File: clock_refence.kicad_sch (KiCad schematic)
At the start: 132 parts, among them J201 REFIN, J202 REFIN_DIRECT_P, J203 REFIN_DIRECT_N, J204 REFOUT_AUX_P, J205 REFOUT_AUX_N, J206 RFShield_TwoPieces, J207 REFOUT, J208 VTUNE, J209 DNP, T201 TC2-1T+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

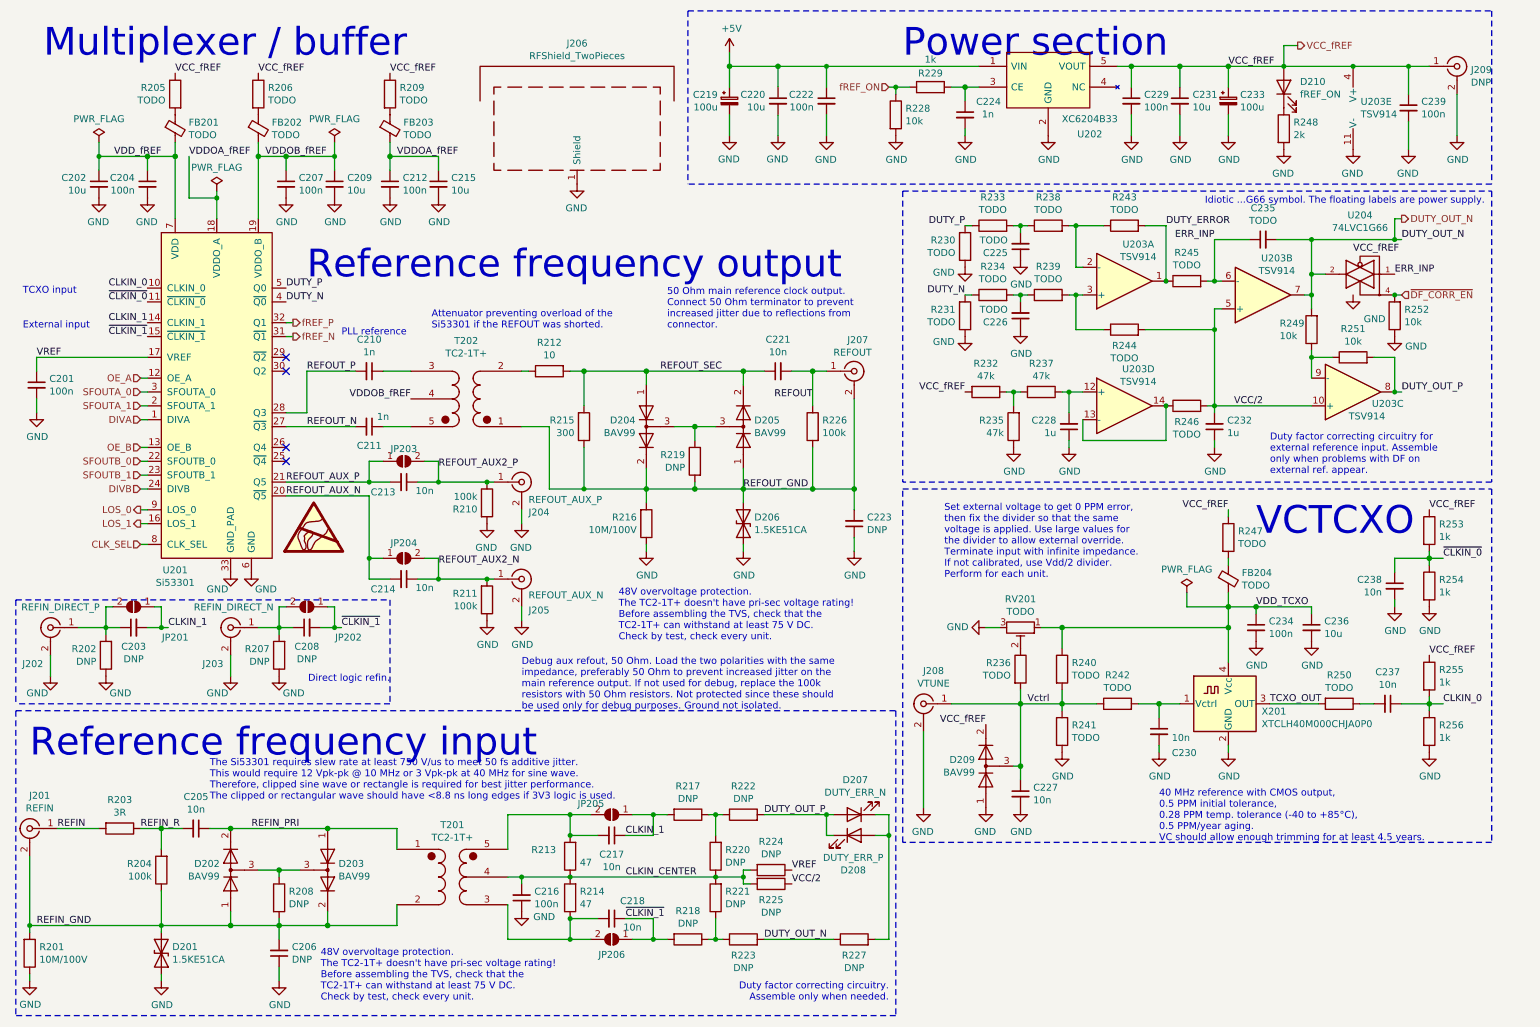
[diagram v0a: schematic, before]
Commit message: Working on making the original module a self-contained module with MCU. Added PCB.
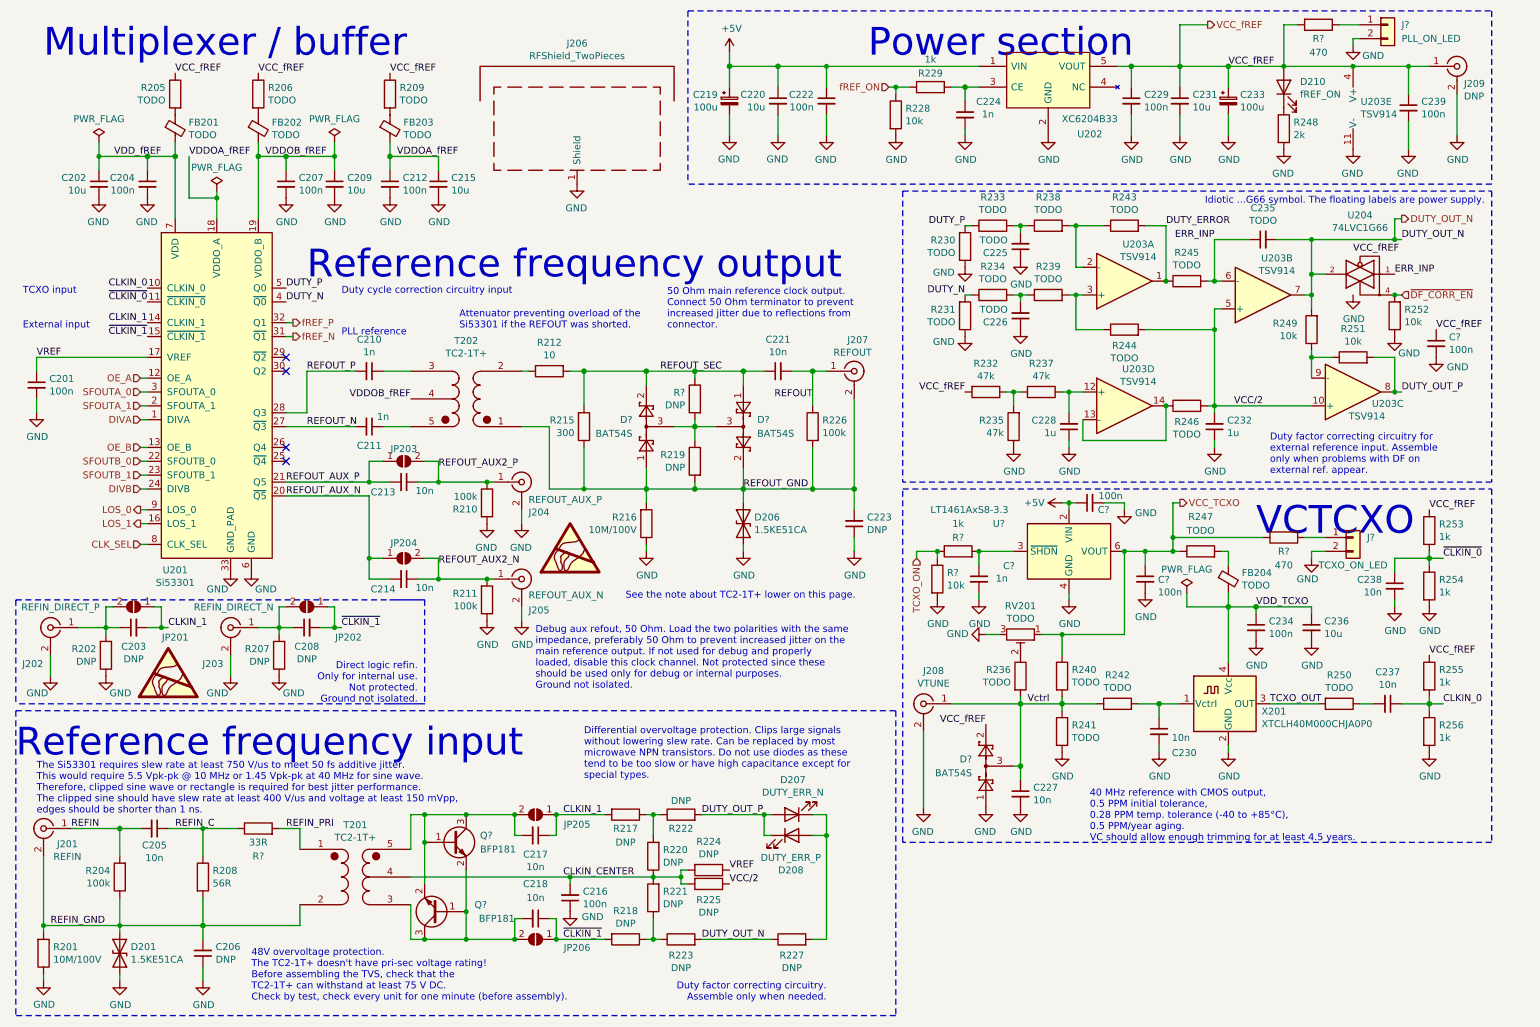
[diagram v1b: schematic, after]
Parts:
- removed D202, D203, D204, D205, D209: BAV99, Package_TO_SOT_SMD:SOT-23, symbol Diode:BAV99
- removed R203: 3R, Resistor_SMD:R_0603_1608Metric_Pad0.98x0.95mm_HandSolder, symbol Device:R
- removed R213, R214: 47, Resistor_SMD:R_0603_1608Metric_Pad0.98x0.95mm_HandSolder, symbol Device:R
- added C?: 1n, Capacitor_SMD:C_0603_1608Metric_Pad1.08x0.95mm_HandSolder, symbol Device:C_Small
- added C? (x3): 100n, Capacitor_SMD:C_0603_1608Metric_Pad1.08x0.95mm_HandSolder, symbol Device:C_Small
- added D? (x3): BAT54S, Package_TO_SOT_SMD:SOT-23, symbol Diode:BAT54S
- added J?: PLL_ON_LED, symbol Connector_Generic:Conn_01x02
- added J?: TCXO_ON_LED, symbol Connector_Generic:Conn_01x02
- added Q? (x2): BFP181, Package_TO_SOT_SMD:SOT-23_Handsoldering, symbol petr:BFP181
- added R?: 33R, Resistor_SMD:R_0603_1608Metric_Pad0.98x0.95mm_HandSolder, symbol Device:R
- added R?: DNP, Resistor_SMD:R_0603_1608Metric_Pad0.98x0.95mm_HandSolder, symbol Device:R
- added R?: 10k, Resistor_SMD:R_0603_1608Metric_Pad0.98x0.95mm_HandSolder, symbol Device:R
- added R? (x2): 470, Resistor_SMD:R_0603_1608Metric_Pad0.98x0.95mm_HandSolder, symbol Device:R
- added R?: 1k, Resistor_SMD:R_0603_1608Metric_Pad0.98x0.95mm_HandSolder, symbol Device:R
- added U?: LT1461AxS8-3.3, Package_SO:SOIC-8_3.9x4.9mm_P1.27mm, symbol Reference_Voltage:LT1461AxS8-3.3
- R208: value DNP -> 56R
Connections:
- net REFIN_R is gone; now on net REFIN: C205.2, R204.2
- net +5V: now also C?.1, U?.2 (VIN)
- net GND: now also C?.2, C?.2, C?.2, C?.2, D?.1, J?.2 (Pin_2), J?.2 (Pin_2), R?.2, U?.4 (GND)
- net REFIN_PRI: now also R?.2; no longer C205.1
- net REFOUT_GND: now also D?.1, D?.2
- net REFOUT_SEC: now also D?.1, D?.2, R?.1
- net VCC: now also C?.1, D?.2, R?.2; no longer R247.1
- net VDD_TCXO: no longer R240.1, RV201.1
- net Vctrl: now also D?.3
- net REFIN_C: now reaches R208.1
- net REFIN_C: now also C205.1, R?.1
- net at C217.2, JP205.2 (B), T201.5 (SB): now also Q?.1 (B), Q?.2 (E), Q?.3 (C)
- net at R219.1: now also D?.3, D?.3, R?.2
- net at C218.2, JP206.2 (B), T201.3 (SA): now also Q?.1 (B), Q?.2 (E), Q?.3 (C)
- net ~CLKIN_0 renamed ~{CLKIN_0}
- net ~CLKIN_1 renamed ~{CLKIN_1}
- net ~DF_CORR_EN renamed ~{DF_CORR_EN}
- new net: J?.1 (Pin_1), R?.1 (x2)
- new net: C?.1, R?.2, U?.3 (~{SHDN})
- new net TCXO_ON: R?.1, R?.1
- new net VCC_TCXO: C?.1, R240.1, R247.1, R?.2, RV201.1, U?.6 (VOUT)
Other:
- note added: "48V overvoltage protection. The TC2-1T+ doesn't have pri-sec voltage rating! Before assembling the TVS, check that the TC2-1T+ can withstand at least 75 V DC. Check by test, check every unit for one minute (before assembly)."
- note added: "Debug aux refout, 50 Ohm. Load the two polarities with the same impedance, preferably 50 Ohm to prevent increased jitter on the main reference output. If not used for debug and properly loaded, disable this clock channel. Not protected since these should be used only for debug or internal purposes. Ground not isolated."
- note added: "Differential overvoltage protection. Clips large signals without lowering slew rate. Can be replaced by most microwave NPN transistors. Do not use diodes as these tend to be too slow or have high capacitance except for special types."
- note added: "Direct logic refin. Only for internal use. Not protected. Ground not isolated."
- note added: "Duty cycle correction circuitry input"
- note added: "See the note about TC2-1T+ lower on this page."
- note added: "The Si53301 requires slew rate at least 750 V/us to meet 50 fs additive jitter. This would require 5.5 Vpk-pk @ 10 MHz or 1.45 Vpk-pk at 40 MHz for sine wave. Therefore, clipped sine wave or rectangle is required for best jitter performance. The clipped sine should have slew rate at least 400 V/us and voltage at least 150 mVpp, edges should be shorter than 1 ns."
- note removed: "48V overvoltage protection. The TC2-1T+ doesn't have pri-sec voltage rating! Before assembling the TVS, check that the TC2-1T+ can withstand at least 75 V DC. Check by test, check every unit."
- note removed: "Debug aux refout, 50 Ohm. Load the two polarities with the same impedance, preferably 50 Ohm to prevent increased jitter on the main reference output. If not used for debug, replace the 100k resistors with 50 Ohm resistors. Not protected since these should be used only for debug purposes. Ground not isolated."
- note removed: "Direct logic refin."
- note removed: "Set external voltage to get 0 PPM error, then fix the divider so that the same voltage is applied. Use large values for the divider to allow external override. Terminate input with infinite impedance. If not calibrated, use Vdd/2 divider. Perform for each unit."
- note removed: "The Si53301 requires slew rate at least 750 V/us to meet 50 fs additive jitter. This would require 12 Vpk-pk @ 10 MHz or 3 Vpk-pk at 40 MHz for sine wave. Therefore, clipped sine wave or rectangle is required for best jitter performance. The clipped or rectangular wave should have <8.8 ns long edges if 3V3 logic is used."
- moved on the sheet: C205, C206, C216, C217, C218, D201, D207, D208, J201, JP205, JP206, R201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

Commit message: Updates to schematic
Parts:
- removed J?: PLL_ON_LED, symbol Connector_Generic:Conn_01x02
- removed R?: 470, Resistor_SMD:R_0603_1608Metric_Pad0.98x0.95mm_HandSolder, symbol Device:R

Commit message: Updated schematics
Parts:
- removed C203, C206, C208: DNP, Capacitor_SMD:C_0603_1608Metric_Pad1.08x0.95mm_HandSolder, symbol Device:C_Small
- removed C205, C217, C218, C227, C230, C237, C238: 10n, Capacitor_SMD:C_0603_1608Metric_Pad1.08x0.95mm_HandSolder, symbol Device:C_Small
- removed C216, C234, C? (x3): 100n, Capacitor_SMD:C_0603_1608Metric_Pad1.08x0.95mm_HandSolder, symbol Device:C_Small
- removed C225, C226, C235: TODO, Capacitor_SMD:C_0603_1608Metric_Pad1.08x0.95mm_HandSolder, symbol Device:C_Small
- removed C228, C232: 1u, Capacitor_SMD:C_0603_1608Metric_Pad1.08x0.95mm_HandSolder, symbol Device:C_Small
- removed C236: 10u, Capacitor_SMD:C_0805_2012Metric_Pad1.18x1.45mm_HandSolder, symbol Device:C_Small
- removed C?: 1n, Capacitor_SMD:C_0603_1608Metric_Pad1.08x0.95mm_HandSolder, symbol Device:C_Small
- removed D201: 1.5KE51CA, Diode_THT:D_DO-201AE_P15.24mm_Horizontal, symbol Diode:1.5KExxCA
- removed D207: DUTY_ERR_N, LED_SMD:LED_0603_1608Metric_Pad1.05x0.95mm_HandSolder, symbol Device:LED
- removed D208: DUTY_ERR_P, LED_SMD:LED_0603_1608Metric_Pad1.05x0.95mm_HandSolder, symbol Device:LED
- removed D?: BAT54S, Package_TO_SOT_SMD:SOT-23, symbol Diode:BAT54S
- removed FB204: TODO, Inductor_SMD:L_0603_1608Metric_Pad1.05x0.95mm_HandSolder, symbol Device:FerriteBead_Small
- removed J201: REFIN, petr_kicad:SMA_rosenberger_hybrid, symbol Connector:Conn_Coaxial
- removed J202: REFIN_DIRECT_P, petr_kicad:SMA_rosenberger_hybrid, symbol Connector:Conn_Coaxial
- removed J203: REFIN_DIRECT_N, petr_kicad:SMA_rosenberger_hybrid, symbol Connector:Conn_Coaxial
- removed J208: VTUNE, petr_kicad:SMA_rosenberger_hybrid, symbol Connector:Conn_Coaxial
- removed J?: TCXO_ON_LED, symbol Connector_Generic:Conn_01x02
- removed JP201, JP202, JP205, JP206: SolderJumper_2_Open, Jumper:SolderJumper-2_P1.3mm_Open_RoundedPad1.0x1.5mm, symbol Jumper:SolderJumper_2_Open
- removed Q? (x2): BFP181, Package_TO_SOT_SMD:SOT-23_Handsoldering, symbol petr:BFP181
- removed R201: 10M/100V, Resistor_SMD:R_1206_3216Metric_Pad1.30x1.75mm_HandSolder, symbol Device:R
- removed R202, R207, R217, R218, R220, R221, R222, R223, R224, R225, R227: DNP, Resistor_SMD:R_0603_1608Metric_Pad0.98x0.95mm_HandSolder, symbol Device:R
- removed R204: 100k, Resistor_SMD:R_0603_1608Metric_Pad0.98x0.95mm_HandSolder, symbol Device:R
- removed R208: 56R, Resistor_SMD:R_0603_1608Metric_Pad0.98x0.95mm_HandSolder, symbol Device:R
- removed R230, R231, R233, R234, R236, R238, R239, R240, R241, R242, R243, R244, R245, R246, R247, R250: TODO, Resistor_SMD:R_0603_1608Metric_Pad0.98x0.95mm_HandSolder, symbol Device:R
- removed R232, R235, R237: 47k, Resistor_SMD:R_0603_1608Metric_Pad0.98x0.95mm_HandSolder, symbol Device:R
- removed R249, R251, R252, R?: 10k, Resistor_SMD:R_0603_1608Metric_Pad0.98x0.95mm_HandSolder, symbol Device:R
- removed R253, R254, R255, R256, R?: 1k, Resistor_SMD:R_0603_1608Metric_Pad0.98x0.95mm_HandSolder, symbol Device:R
- removed R?: 33R, Resistor_SMD:R_0603_1608Metric_Pad0.98x0.95mm_HandSolder, symbol Device:R
- removed R?: 470, Resistor_SMD:R_0603_1608Metric_Pad0.98x0.95mm_HandSolder, symbol Device:R
- removed RV201: TODO, Potentiometer_THT:Potentiometer_Bourns_3296Y_Vertical, symbol Device:R_Potentiometer_Trim
- removed T201: TC2-1T+, Transformer_SMD:Transformer_MACOM_SM-22, symbol petr_lib_nightly:TC2-1T+
- removed U203: TSV914, Package_SO:SOIC-14_3.9x8.7mm_P1.27mm, symbol Amplifier_Operational:TSV914
- removed U204: 74LVC1G66, Package_TO_SOT_SMD:SOT-353_SC-70-5_Handsoldering, symbol 74xGxx:74LVC1G66
- removed U?: LT1461AxS8-3.3, Package_SO:SOIC-8_3.9x4.9mm_P1.27mm, symbol Reference_Voltage:LT1461AxS8-3.3
- removed X201: XTCLH40M000CHJA0P0, Oscillator:Oscillator_SMD_Fordahl_DFAS15-4Pin_5.0x3.2mm_HandSoldering, symbol petr_lib_nightly:XTCLH40M000CHJA0P0
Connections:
- net VCC renamed VCC_fREF
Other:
- added sheet Input Clocks (input_clocks.kicad_sch)
- note added: "External output"
- note added: "Internal clock"
- note added: "Loss of signal"
- note removed: "40 MHz reference with CMOS output, 0.5 PPM initial tolerance, 0.28 PPM temp. tolerance (-40 to +85°C), 0.5 PPM/year aging. VC should allow enough trimming for at least 4.5 years."
- note removed: "48V overvoltage protection. The TC2-1T+ doesn't have pri-sec voltage rating! Before assembling the TVS, check that the TC2-1T+ can withstand at least 75 V DC. Check by test, check every unit for one minute (before assembly)."
- note removed: "Differential overvoltage protection. Clips large signals without lowering slew rate. Can be replaced by most microwave NPN transistors. Do not use diodes as these tend to be too slow or have high capacitance except for special types."
- note removed: "Direct logic refin. Only for internal use. Not protected. Ground not isolated."
- note removed: "Duty factor correcting circuitry for external reference input. Assemble only when problems with DF on external ref. appear."
- note removed: "Duty factor correcting circuitry. Assemble only when needed."
- note removed: "Idiotic ...G66 symbol. The floating labels are power supply."
- note removed: "Reference frequency input"
- note removed: "The Si53301 requires slew rate at least 750 V/us to meet 50 fs additive jitter. This would require 5.5 Vpk-pk @ 10 MHz or 1.45 Vpk-pk at 40 MHz for sine wave. Therefore, clipped sine wave or rectangle is required for best jitter performance. The clipped sine should have slew rate at least 400 V/us and voltage at least 150 mVpp, edges should be shorter than 1 ns."
- note removed: "VCTCXO"
- moved on the sheet: C201, C202, C204, C207, C209, C210, C211, C212, C213, C214, C215, C219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

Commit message: Updated schematics
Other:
- sheet Input Clocks ports: added CLKIN_0, CLKIN_1, DUTY_N, DUTY_OUT_N, DUTY_P, TCXO_ON, VCC_TCXO, VCC_fREF, ~{CLKIN_0}, ~{CLKIN_1}, ~{DF_CORR_EN}; removed none
- moved on the sheet: C201, C202, C204, C207, C209, C210, C211, C212, C213, C214, C215, C221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

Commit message: Finished schematics
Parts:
- gave numbers to parts that had none: 3
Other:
- moved on the sheet: C221, C223, D202, D203, D206, J207, R203, R212, R215, R216, R219, R226
